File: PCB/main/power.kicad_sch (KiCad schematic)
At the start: 21 parts, among them Q2 Q_PMOS_SGD, U1 LP2951-33DR, U8 AMS1117

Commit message: Updated BOM
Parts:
- C1, C10: JLC Part # (none) -> C1525; Price (none) -> 0.0011
- C11: footprint (none) -> Capacitor_SMD:C_1206_3216Metric; JLC Part # (none) -> C15008; Price (none) -> 0.1135
- C2: JLC Part # (none) -> C59461; Price (none) -> 0.0098
- C3: value 300pF -> 330pF; JLC Part # (none) -> C13533; Price (none) -> 0.0053
- D1: JLC Part # (none) -> C408389; Price (none) -> 0.0148
- D2: footprint (none) -> Footprint_EEE3088F:LL-34_L3.5-W1.5-RD; JLC Part # (none) -> C8061; Price (none) -> 0.0182
- D3: value DIODE -> DIODE-FIIXIXINXIXNVX; footprint Diode_SMD:D_SMA -> (none); JLC Part # (none) -> C95872
- Q2: footprint (none) -> Package_TO_SOT_SMD:SOT-23; symbol Device:Q_PMOS_SGD -> Device:Q_PMOS_GSD; JLC Part # (none) -> C15127; Price (none) -> 0.1774
- R1: footprint Resistor_SMD:R_0402_1005Metric -> Resistor_SMD:R_0805_2012Metric; JLC Part # (none) -> C26112; Price (none) -> 0.0043
- R19: footprint (none) -> Resistor_SMD:R_0603_1608Metric; JLC Part # (none) -> C22775; Price (none) -> 0.0013
- R2: JLC Part # (none) -> C375495; Price (none) -> 0.0007
- RV1: JLC Part # (none) -> C145161; Price (none) -> 0.086
- U1: JLC Part # (none) -> C109381; Price (none) -> 0.5873
- U8: JLC Part # (none) -> C6186; Price (none) -> 0.1855
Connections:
- net +5V (INPUT PROTECTED): now also Q2.2 (S); no longer Q2.1 (S)
- net at D2.2 (A), R19.1: now also Q2.1 (G); no longer Q2.2 (G)
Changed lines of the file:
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@@
       (effects (font (size 1.27 1.27)) (justify left))
     )
-    (property "Footprint" "" (id 2) (at 234.0102 137.795 0)
+    (property "Footprint" "Capacitor_SMD:C_1206_3216Metric" (id 2) (at 234.0102 137.795 0)
       (effects (font (size 1.27 1.27)) hide)
     )
@@
       (effects (font (size 1.27 1.27)) hide)
     )
-    (pin "1")
-    (pin "2")
-  )
-  (symbol (lib_id "Device:Q_PMOS_SGD") (at 78.74 90.17 90) (unit 1)
+    (property "JLC Part #" "C15008" (id 4) (at 233.045 133.985 0)
+      (effects (font (size 1.27 1.27)) hide)
+    )
+    (property "Price" "0.1135" (id 5) (at 233.045 133.985 0)
+      (effects (font (size 1.27 1.27)) hide)
+    )
+    (pin "1")
+    (pin "2")
+  )
+  (symbol (lib_id "Device:Q_PMOS_GSD") (at 78.74 90.17 90) (unit 1)
     (in_bom yes) (on_board yes) (fields_autoplaced)
     (property "Reference" "Q2" (id 0) (at 78.74 80.01 90))
     (property "Value" "Q_PMOS_SGD" (id 1) (at 78.74 82.55 90))
-    (property "Footprint" "" (id 2) (at 76.2 85.09 0)
+    (property "Footprint" "Package_TO_SOT_SMD:SOT-23" (id 2) (at 76.2 85.09 0)
       (effects (font (size 1.27 1.27)) hide)
     )
@@
       (effects (font (size 1.27 1.27)) hide)
     )
+    (property "JLC Part #" "C15127" (id 4) (at 78.74 90.17 0)
+      (effects (font (size 1.27 1.27)) hide)
+    )
+    (property "Price" "0.1774" (id 5) (at 78.74 90.17 0)
+      (effects (font (size 1.27 1.27)) hide)
+    )
     (pin "1")
     (pin "2")
@@
     )
     (property "Datasheet" "~" (id 3) (at 107.95 149.86 0)
+      (effects (font (size 1.27 1.27)) hide)
+    )
+    (property "JLC Part #" "C375495" (id 4) (at 107.95 149.86 0)
+      (effects (font (size 1.27 1.27)) hide)
+    )
+    (property "Price" "0.0007" (id 5) (at 107.95 149.86 0)
       (effects (font (size 1.27 1.27)) hide)
     )
@@
       (effects (font (size 1.27 1.27)) hide)
     )
+    (property "JLC Part #" "C59461 " (id 4) (at 77.47 156.21 0)
+      (effects (font (size 1.27 1.27)) hide)
+    )
+    (property "Price" "0.0098" (id 5) (at 77.47 156.21 0)
+      (effects (font (size 1.27 1.27)) hide)
+    )
     (pin "1")
     (pin "2")
@@
       (effects (font (size 1.27 1.27)) (justify left))
     )
-    (property "Footprint" "" (id 2) (at 88.9 91.44 0)
+    (property "Footprint" "Footprint_EEE3088F:LL-34_L3.5-W1.5-RD" (id 2) (at 88.9 91.44 0)
       (effects (font (size 1.27 1.27)) hide)
     )
     (property "Datasheet" "~" (id 3) (at 88.9 91.44 0)
+      (effects (font (size 1.27 1.27)) hide)
+    )
+    (property "JLC Part #" "C8061" (id 4) (at 88.9 91.44 0)
+      (effects (font (size 1.27 1.27)) hide)
+    )
+    (property "Price" "0.0182" (id 5) (at 88.9 91.44 0)
       (effects (font (size 1.27 1.27)) hide)
     )
@@
       (effects (font (size 1.27 1.27)) hide)
     )
+    (property "JLC Part #" "C6186" (id 4) (at 220.98 126.365 0)
+      (effects (font (size 1.27 1.27)) hide)
+    )
+    (property "Price" "0.1855" (id 5) (at 220.98 126.365 0)
+      (effects (font (size 1.27 1.27)) hide)
+    )
     (pin "1")
     (pin "2")
@@
     )
     (property "Datasheet" "http://www.ti.com/lit/ds/symlink/lp2951.pdf" (id 3) (at 54.61 129.54 0)
+      (effects (font (size 1.27 1.27)) hide)
+    )
+    (property "JLC Part #" "C109381" (id 4) (at 60.96 140.97 0)
+      (effects (font (size 1.27 1.27)) hide)
+    )
+    (property "Price" "0.5873" (id 5) (at 60.96 140.97 0)
       (effects (font (size 1.27 1.27)) hide)
     )
@@
       (effects (font (size 1.27 1.27)) hide)
     )
+    (property "JLC Part #" "C408389" (id 4) (at 64.77 66.04 0)
+      (effects (font (size 1.27 1.27)) hide)
+    )
+    (property "Price" "0.0148" (id 5) (at 64.77 66.04 0)
+      (effects (font (size 1.27 1.27)) hide)
+    )
     (pin "1")
     (pin "2")
@@
       (effects (font (size 1.27 1.27)) hide)
     )
-    (property "Datasheet" "~" (id 3) (at 211.455 133.985 0)
+    (property "Datasheet" "" (id 3) (at 211.455 133.985 0)
+      (effects (font (size 1.27 1.27)) hide)
+    )
+    (property "JLC Part #" "C1525" (id 4) (at 211.455 133.985 0)
+      (effects (font (size 1.27 1.27)) hide)
+    )
+    (property "Price" "0.0011" (id 5) (at 211.455 133.985 0)
       (effects (font (size 1.27 1.27)) hide)
     )
@@
     (in_bom yes) (on_board yes) (fields_autoplaced)
     (property "Reference" "D3" (id 0) (at 83.82 128.3802 0))
-    (property "Value" "DIODE" (id 1) (at 83.82 130.9171 0))
-    (property "Footprint" "Diode_SMD:D_SMA" (id 2) (at 83.82 133.35 0)
+    (property "Value" "DIODE-FIIXIXINXIXNVX" (id 1) (at 83.82 130.9171 0))
+    (property "Footprint" "" (id 2) (at 83.82 133.35 0)
       (effects (font (size 1.27 1.27)) hide)
     )
@@
       (effects (font (size 1.27 1.27)) (justify left) hide)
     )
+    (property "JLC Part #" "C95872" (id 6) (at 83.82 133.35 0)
+      (effects (font (size 1.27 1.27)) hide)
+    )
     (pin "1")
     (pin "2")
@@
       (effects (font (size 1.27 1.27)) hide)
     )
+    (property "JLC Part #" "C145161" (id 4) (at 107.95 162.56 0)
+      (effects (font (size 1.27 1.27)) hide)
+    )
+    (property "Price" "0.086" (id 5) (at 107.95 162.56 0)
+      (effects (font (size 1.27 1.27)) hide)
+    )
     (pin "1")
     (pin "2")
@@
       (effects (font (size 1.27 1.27)) (justify left))
     )
-    (property "Footprint" "Resistor_SMD:R_0402_1005Metric" (id 2) (at 106.172 138.43 90)
+    (property "Footprint" "Resistor_SMD:R_0805_2012Metric" (id 2) (at 106.172 138.43 90)
       (effects (font (size 1.27 1.27)) hide)
     )
@@
       (effects (font (size 1.27 1.27)) hide)
     )
+    (property "JLC Part #" "C26112" (id 4) (at 107.95 138.43 0)
+      (effects (font (size 1.27 1.27)) hide)
+    )
+    (property "Price" "0.0043" (id 5) (at 107.95 138.43 0)
+      (effects (font (size 1.27 1.27)) hide)
+    )
     (pin "1")
     (pin "2")
@@
       (effects (font (size 1.27 1.27)) (justify left))
     )
-    (property "Footprint" "" (id 2) (at 76.962 100.33 90)
+    (property "Footprint" "Resistor_SMD:R_0603_1608Metric" (id 2) (at 76.962 100.33 90)
       (effects (font (size 1.27 1.27)) hide)
     )
     (property "Datasheet" "~" (id 3) (at 78.74 100.33 0)
+      (effects (font (size 1.27 1.27)) hide)
+    )
+    (property "JLC Part #" "C22775" (id 4) (at 78.74 100.33 0)
+      (effects (font (size 1.27 1.27)) hide)
+    )
+    (property "Price" "0.0013" (id 5) (at 78.74 100.33 0)
       (effects (font (size 1.27 1.27)) hide)
     )
@@
       (effects (font (size 1.27 1.27)) hide)
     )
-    (property "Datasheet" "~" (id 3) (at 38.1 156.21 0)
+    (property "Datasheet" "" (id 3) (at 38.1 156.21 0)
+      (effects (font (size 1.27 1.27)) hide)
+    )
+    (property "JLC Part #" "C1525" (id 4) (at 38.1 156.21 0)
+      (effects (font (size 1.27 1.27)) hide)
+    )
+    (property "Price" "0.0011" (id 5) (at 38.1 156.21 0)
       (effects (font (size 1.27 1.27)) hide)
     )
@@
       (effects (font (size 1.27 1.27)) (justify left))
     )
-    (property "Value" "300pF" (id 1) (at 96.52 139.6999 0)
+    (property "Value" "330pF" (id 1) (at 96.52 139.6999 0)
       (effects (font (size 1.27 1.27)) (justify left))
     )
@@
       (effects (font (size 1.27 1.27)) hide)
     )
+    (property "JLC Part #" "C13533" (id 4) (at 92.71 138.43 0)
+      (effects (font (size 1.27 1.27)) hide)
+    )
+    (property "Price" "0.0053" (id 5) (at 92.71 138.43 0)
+      (effects (font (size 1.27 1.27)) hide)
+    )

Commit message: pmosfet name
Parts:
- Q2: value Q_PMOS_SGD -> AO3401A
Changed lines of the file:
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@@
   (symbol (lib_id "Device:Q_PMOS_GSD") (at 78.74 90.17 90) (unit 1)
     (in_bom yes) (on_board yes) (fields_autoplaced)
-    (property "Reference" "Q2" (id 0) (at 78.74 80.01 90))
-    (property "Value" "Q_PMOS_SGD" (id 1) (at 78.74 82.55 90))
+    (property "Reference" "Q2" (id 0) (at 78.74 82.0252 90))
+    (property "Value" "AO3401A" (id 1) (at 78.74 84.5621 90))
     (property "Footprint" "Package_TO_SOT_SMD:SOT-23" (id 2) (at 76.2 85.09 0)
       (effects (font (size 1.27 1.27)) hide)

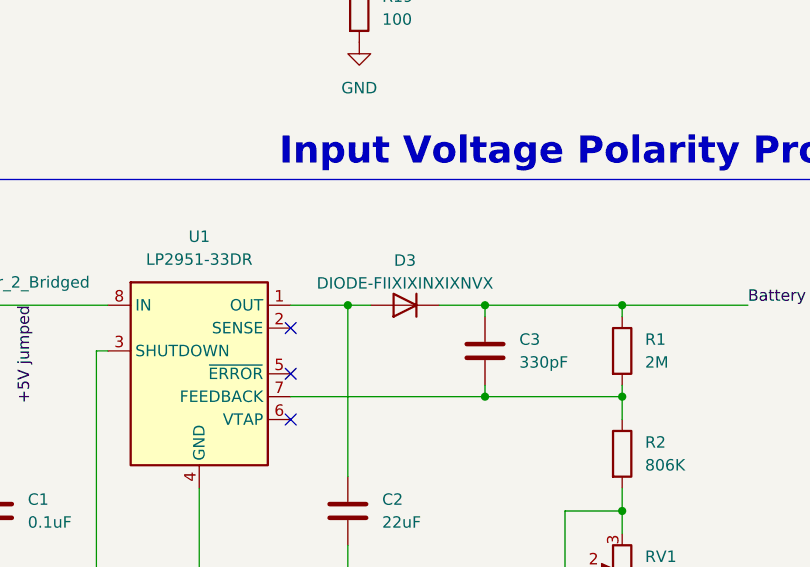
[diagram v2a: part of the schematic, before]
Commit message: Add footprints and test points
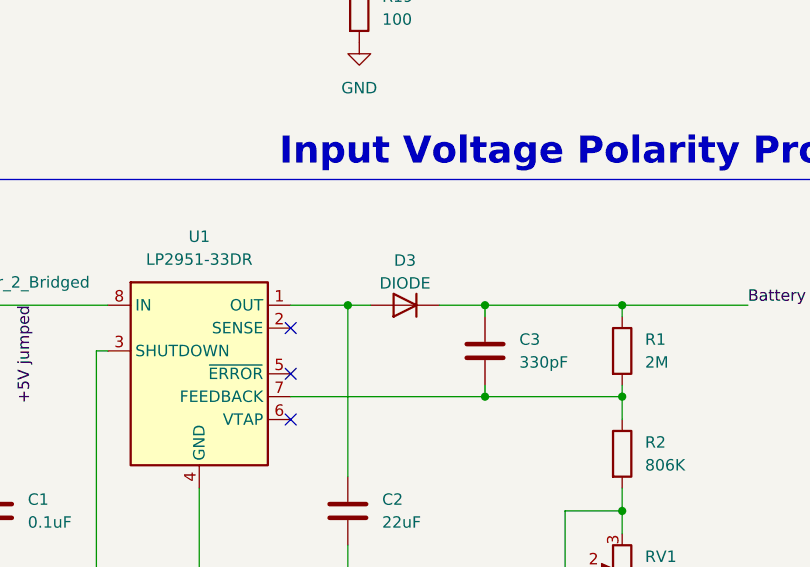
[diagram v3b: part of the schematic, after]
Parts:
- D3: value DIODE-FIIXIXINXIXNVX -> DIODE; footprint (none) -> Footprint_EEE3088F:DO-214AC_L4.3-W2.7-LS5.3-RD; Price (none) -> 0.0089
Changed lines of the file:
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@@
     (in_bom yes) (on_board yes) (fields_autoplaced)
     (property "Reference" "D3" (id 0) (at 83.82 128.3802 0))
-    (property "Value" "DIODE-FIIXIXINXIXNVX" (id 1) (at 83.82 130.9171 0))
-    (property "Footprint" "" (id 2) (at 83.82 133.35 0)
+    (property "Value" "DIODE" (id 1) (at 83.82 130.9171 0))
+    (property "Footprint" "Footprint_EEE3088F:DO-214AC_L4.3-W2.7-LS5.3-RD" (id 2) (at 83.82 133.35 0)
       (effects (font (size 1.27 1.27)) hide)
     )
@@
       (effects (font (size 1.27 1.27)) hide)
     )
+    (property "Price" "0.0089" (id 7) (at 83.82 133.35 0)
+      (effects (font (size 1.27 1.27)) hide)
+    )

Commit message: Design PCB
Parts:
- removed JP5: SolderJumper_2_Bridged, Jumper:SolderJumper-2_P1.3mm_Bridged2Bar_Pad1.0x1.5mm, symbol Jumper:SolderJumper_2_Bridged
- added TP1, TP2: TestPoint, TestPoint:TestPoint_Pad_D1.0mm, symbol Connector:TestPoint
- renumbered C10 to C4, C11 to C5, D3 to D2, D2 to D3, JP3 to JP2, JP2 to JP3, JP7 to JP4, Q2 to Q1, R19 to R1, R1 to R2, R2 to R3, U8 to U2
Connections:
- net +3.3V: now also TP2.1
- net +5V (REVERSE PROTECTED): now also TP1.1
- net GND: now also BT1.2 (-)
